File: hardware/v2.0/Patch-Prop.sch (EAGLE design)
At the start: 47 parts, among them IC1 TPS77033, IC2 XBEE, IC3 MMA8452Q, IC4 ATMEGA168, IC5 MCP1253, IC6 W2RV005RM, U2 MCP73831, X1 USBSMD

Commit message: Tweaking route style and doing cleanup
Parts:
- renumbered D1 to MOCW
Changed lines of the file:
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@@
 <part name="SUPPLY7" library="supply2" deviceset="V+" device=""/>
 <part name="SUPPLY8" library="supply2" deviceset="V+" device=""/>
-<part name="D1" library="led" deviceset="LED" device="CHIPLED_0805"/>
+<part name="MOCW" library="led" deviceset="LED" device="CHIPLED_0805"/>
 <part name="R2" library="rcl" deviceset="R-US_" device="R0603" value="470"/>
 <part name="R4" library="rcl" deviceset="R-US_" device="R0603" value="2k"/>
@@
 <instance part="SUPPLY7" gate="1" x="401.32" y="129.54"/>
 <instance part="SUPPLY8" gate="1" x="515.62" y="106.68"/>
-<instance part="D1" gate="G$1" x="81.28" y="345.44" rot="R90"/>
+<instance part="MOCW" gate="G$1" x="81.28" y="345.44" rot="R90"/>
 <instance part="R2" gate="G$1" x="93.98" y="345.44" rot="R180"/>
 <instance part="R4" gate="G$1" x="132.08" y="327.66" rot="R270"/>
@@
 <pinref part="U2" gate="G$1" pin="VIN"/>
 <pinref part="C16" gate="G$1" pin="1"/>
-<pinref part="D1" gate="G$1" pin="A"/>
+<pinref part="MOCW" gate="G$1" pin="A"/>
 <wire x1="78.74" y1="345.44" x2="76.2" y2="345.44" width="0.1524" layer="91"/>
 <wire x1="76.2" y1="345.44" x2="76.2" y2="337.82" width="0.1524" layer="91"/>
@@
 <segment>
 <wire x1="88.9" y1="345.44" x2="86.36" y2="345.44" width="0.1524" layer="91"/>
-<pinref part="D1" gate="G$1" pin="C"/>
+<pinref part="MOCW" gate="G$1" pin="C"/>
 <pinref part="R2" gate="G$1" pin="2"/>
 </segment>

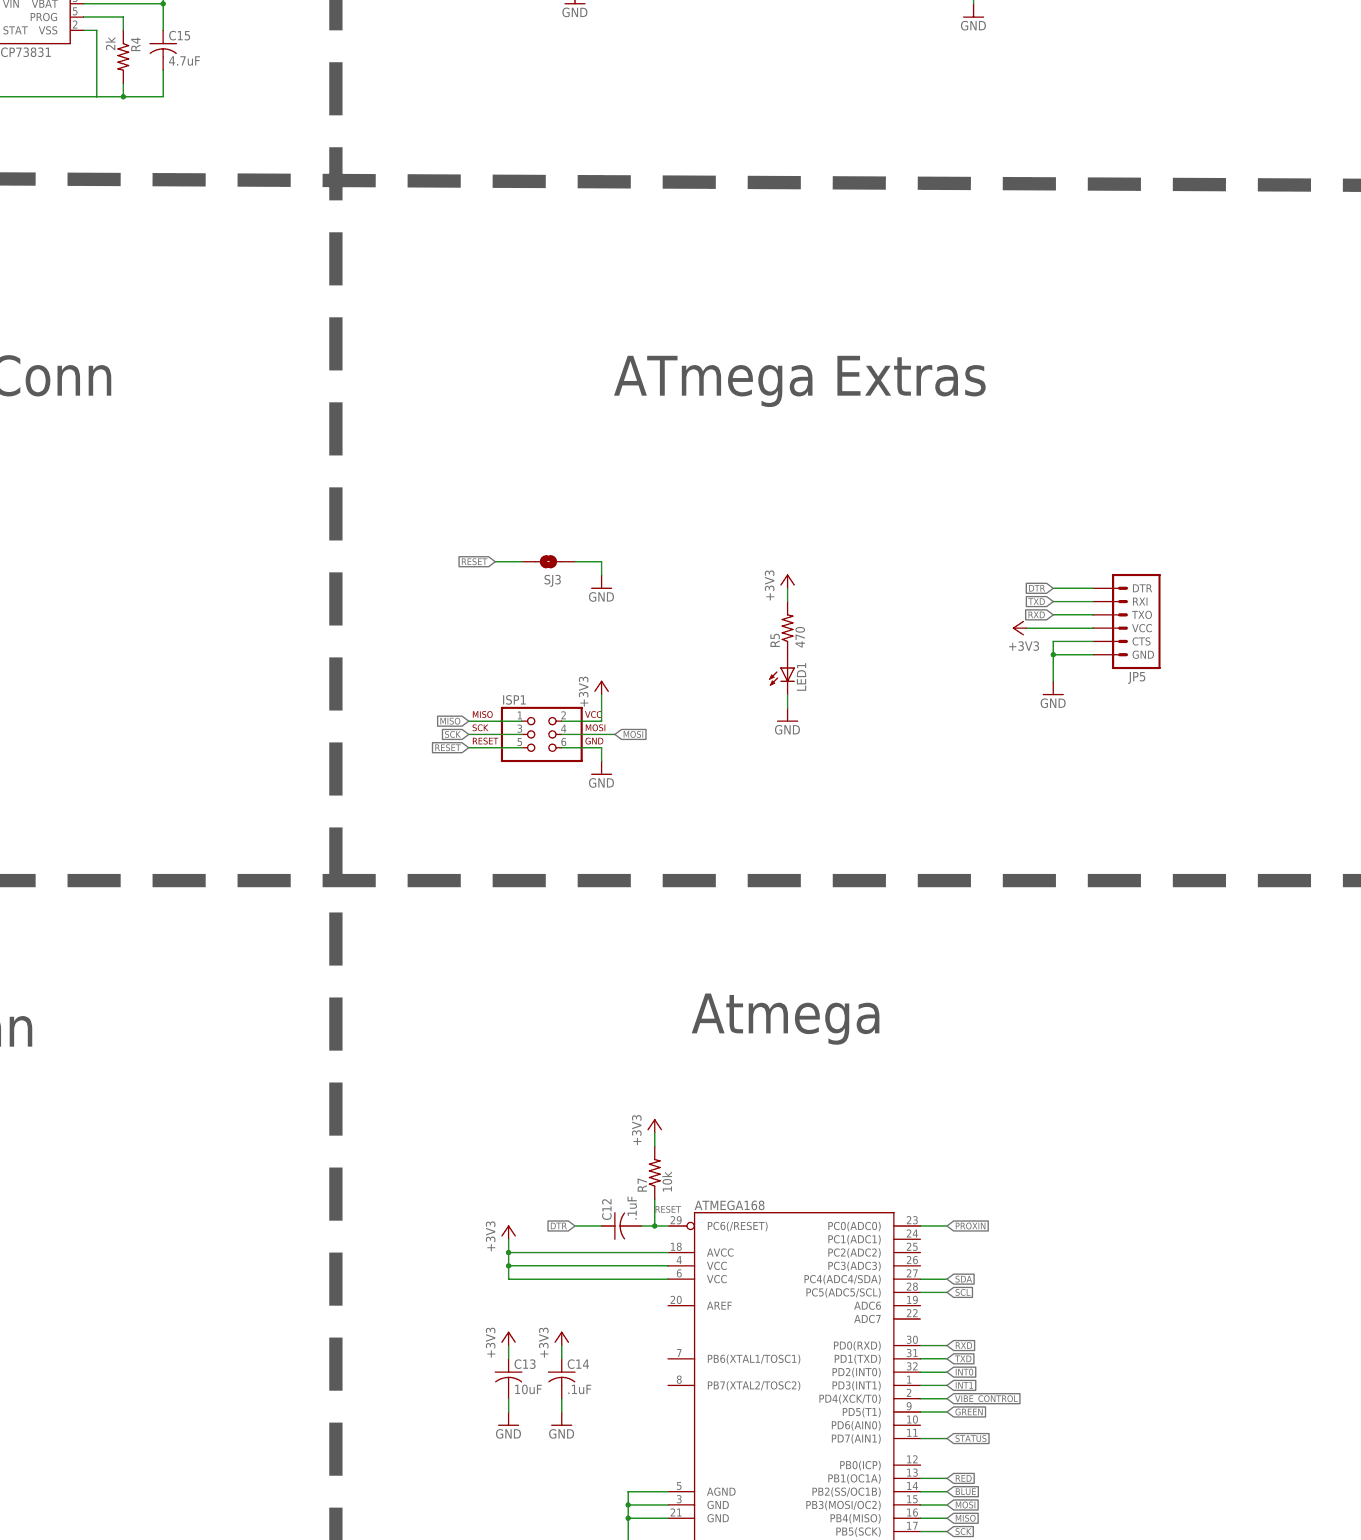
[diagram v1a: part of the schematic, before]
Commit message: Expanded board to fit mounting holes. Used extra space for breakout pins
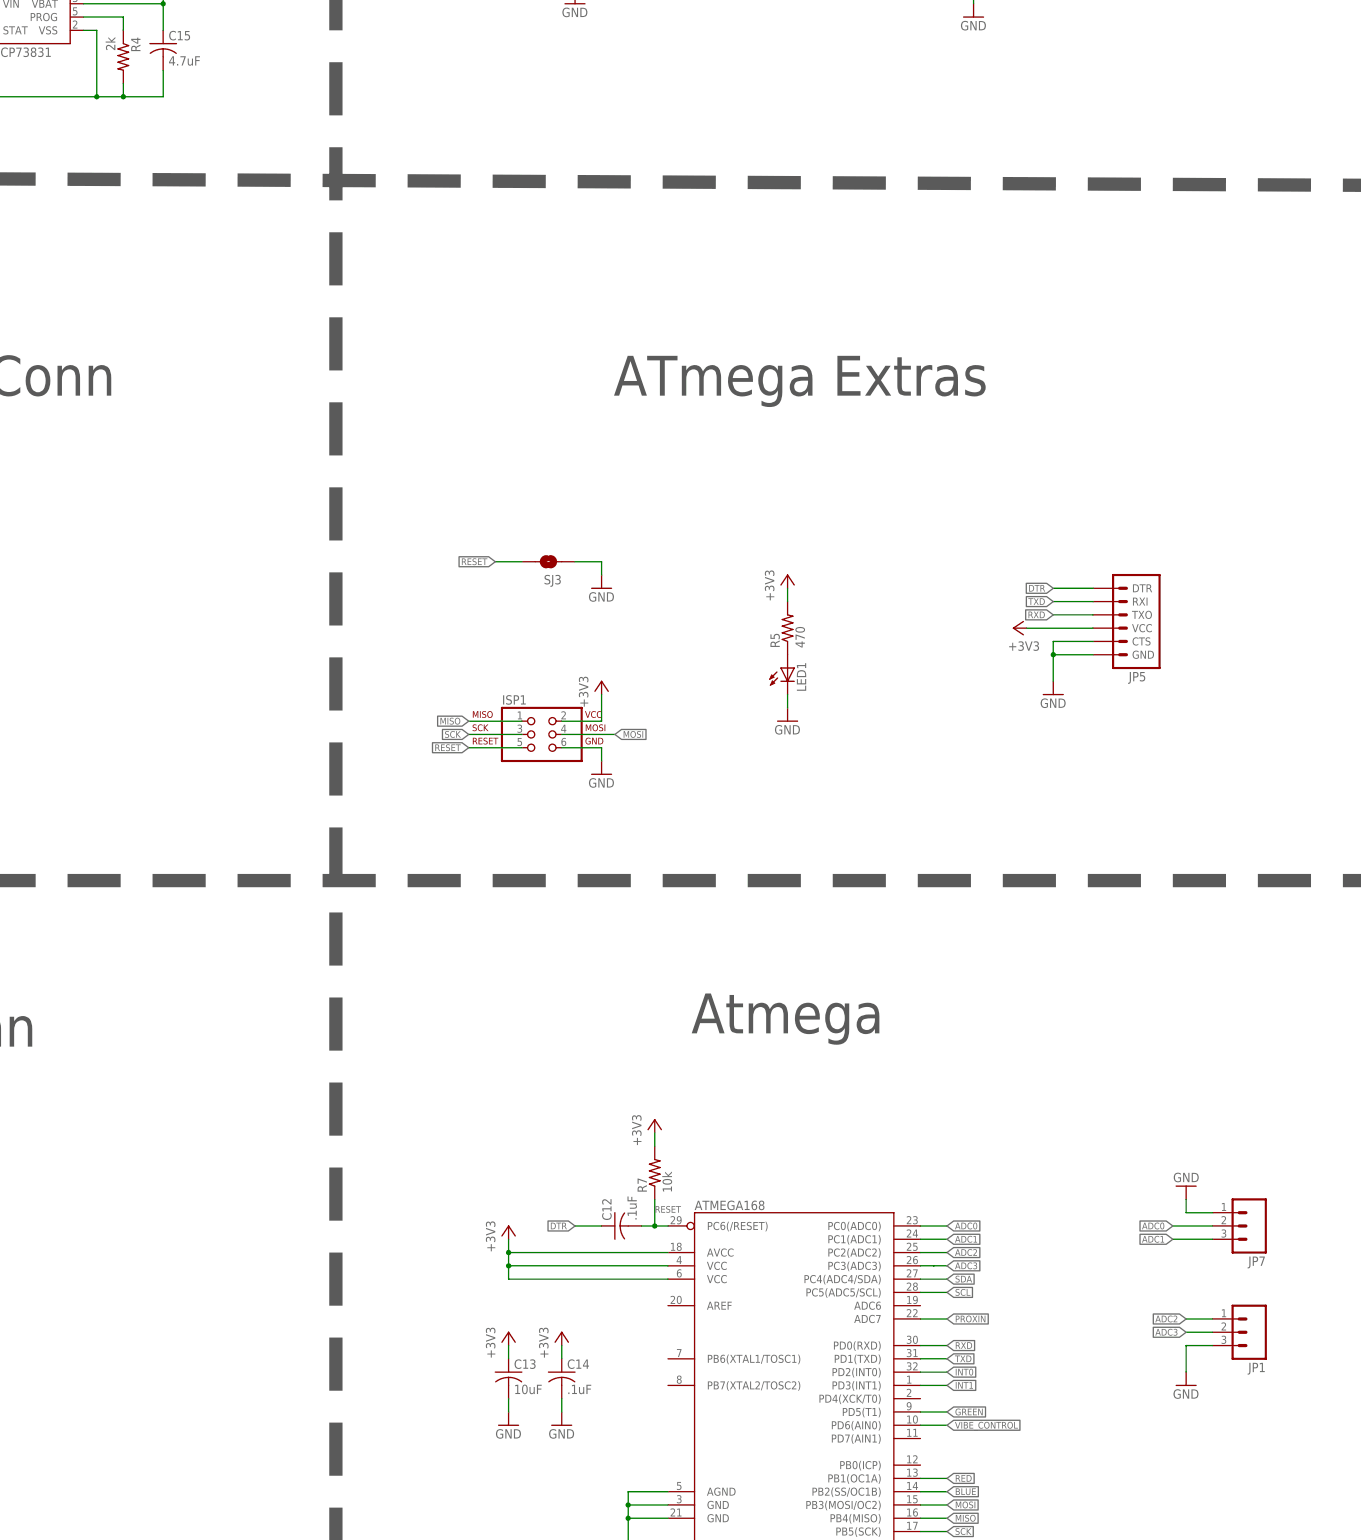
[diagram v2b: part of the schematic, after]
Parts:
- added JP1, JP7: (no value), SparkFun:M03PTH
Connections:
- removed net STATUS: IC4.PD7(AIN1)
- new net ADC0: IC4.PC0(ADC0), JP7.2
- new net ADC1: IC4.PC1(ADC1), JP7.3
- new net ADC2: IC4.PC2(ADC2), JP1.1
- new net ADC3: IC4.PC3(ADC3), JP1.2
- net GND: now also JP1.3, JP7.1
- net PROXIN: now also IC4.ADC7; no longer IC4.PC0(ADC0)
- net VIBE_CONTROL: now also IC4.PD6(AIN0); no longer IC4.PD4(XCK/T0)
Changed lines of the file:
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@@
 <part name="R9" library="rcl" deviceset="R-US_" device="R0603" value="4.7k"/>
 <part name="R10" library="rcl" deviceset="R-US_" device="R0603" value="4.7k"/>
+<part name="JP7" library="SparkFun" deviceset="M03" device="PTH"/>
+<part name="GND2" library="supply1" deviceset="GND" device=""/>
+<part name="JP1" library="SparkFun" deviceset="M03" device="PTH"/>
+<part name="GND3" library="supply1" deviceset="GND" device=""/>
 </parts>
 <sheets>
@@
 <instance part="R9" gate="G$1" x="467.36" y="88.9" rot="R180"/>
 <instance part="R10" gate="G$1" x="467.36" y="93.98" rot="R180"/>
+<instance part="JP7" gate="G$1" x="347.98" y="104.14" rot="R180"/>
+<instance part="GND2" gate="1" x="335.28" y="111.76" rot="R180"/>
+<instance part="JP1" gate="G$1" x="347.98" y="83.82" rot="R180"/>
+<instance part="GND3" gate="1" x="335.28" y="73.66"/>
 </instances>
 <busses>
@@
 <pinref part="U2" gate="G$1" pin="VSS"/>
 <wire x1="127" y1="332.74" x2="127" y2="320.04" width="0.1524" layer="91"/>
+<junction x="127" y="320.04"/>
 </segment>
 <segment>
@@
 <pinref part="GND10" gate="1" pin="GND"/>
 <wire x1="88.9" y1="78.74" x2="88.9" y2="76.2" width="0.1524" layer="91"/>
+</segment>
+<segment>
+<pinref part="JP7" gate="G$1" pin="1"/>
+<pinref part="GND2" gate="1" pin="GND"/>
+<wire x1="340.36" y1="106.68" x2="335.28" y2="106.68" width="0.1524" layer="91"/>
+<wire x1="335.28" y1="106.68" x2="335.28" y2="109.22" width="0.1524" layer="91"/>
+</segment>
+<segment>
+<pinref part="JP1" gate="G$1" pin="3"/>
+<wire x1="340.36" y1="81.28" x2="335.28" y2="81.28" width="0.1524" layer="91"/>
+<wire x1="335.28" y1="81.28" x2="335.28" y2="76.2" width="0.1524" layer="91"/>
+<pinref part="GND3" gate="1" pin="GND"/>
 </segment>
 </net>
@@
 </segment>
 </net>
-<net name="STATUS" class="0">
-<segment>
-<pinref part="IC4" gate="G$1" pin="PD7(AIN1)"/>
-<wire x1="284.48" y1="63.5" x2="289.56" y2="63.5" width="0.1524" layer="91"/>
-<label x="289.56" y="63.5" size="1.27" layer="95" font="vector" ratio="15" xref="yes"/>
-</segment>
-</net>
 <net name="MOSI" class="0">
 <segment>
@@
 </segment>
 <segment>
-<pinref part="IC4" gate="G$1" pin="PC0(ADC0)"/>
-<wire x1="284.48" y1="104.14" x2="289.56" y2="104.14" width="0.1524" layer="91"/>
-<label x="289.56" y="104.14" size="1.27" layer="95" font="vector" ratio="15" xref="yes"/>
+<pinref part="IC4" gate="G$1" pin="ADC7"/>
+<wire x1="284.48" y1="86.36" x2="289.56" y2="86.36" width="0.1524" layer="91"/>
+<label x="289.56" y="86.36" size="1.27" layer="95" font="vector" ratio="15" xref="yes"/>
 </segment>
 </net>
@@
 </segment>
 <segment>
-<pinref part="IC4" gate="G$1" pin="PD4(XCK/T0)"/>
-<wire x1="284.48" y1="71.12" x2="289.56" y2="71.12" width="0.1524" layer="91"/>
-<label x="289.56" y="71.12" size="1.27" layer="95" font="vector" ratio="14" xref="yes"/>
+<pinref part="IC4" gate="G$1" pin="PD6(AIN0)"/>
+<wire x1="284.48" y1="66.04" x2="289.56" y2="66.04" width="0.1524" layer="91"/>
+<label x="289.56" y="66.04" size="1.27" layer="95" font="vector" ratio="15" xref="yes"/>
 </segment>
 </net>
@@
 </segment>
 </net>
+<net name="ADC1" class="0">
+<segment>
+<pinref part="JP7" gate="G$1" pin="3"/>
+<label x="332.74" y="101.6" size="1.27" layer="95" font="vector" ratio="15" rot="R180" xref="yes"/>
+<wire x1="332.74" y1="101.6" x2="340.36" y2="101.6" width="0.1524" layer="91"/>
+</segment>
+<segment>
+<pinref part="IC4" gate="G$1" pin="PC1(ADC1)"/>
+<wire x1="284.48" y1="101.6" x2="289.56" y2="101.6" width="0.1524" layer="91"/>
+<label x="289.56" y="101.6" size="1.27" layer="95" font="vector" ratio="15" xref="yes"/>
+</segment>
+</net>
+<net name="ADC0" class="0">
+<segment>
+<pinref part="JP7" gate="G$1" pin="2"/>
+<wire x1="340.36" y1="104.14" x2="332.74" y2="104.14" width="0.1524" layer="91"/>
+<label x="332.74" y="104.14" size="1.27" layer="95" font="vector" ratio="15" rot="R180" xref="yes"/>
+</segment>
+<segment>
+<pinref part="IC4" gate="G$1" pin="PC0(ADC0)"/>
+<wire x1="289.56" y1="104.14" x2="284.48" y2="104.14" width="0.1524" layer="91"/>
+<label x="289.56" y="104.14" size="1.27" layer="95" font="vector" ratio="15" xref="yes"/>
+</segment>
+</net>
+<net name="ADC2" class="0">
+<segment>
+<pinref part="IC4" gate="G$1" pin="PC2(ADC2)"/>
+<wire x1="284.48" y1="99.06" x2="289.56" y2="99.06" width="0.1524" layer="91"/>
+<label x="289.56" y="99.06" size="1.27" layer="95" font="vector" ratio="15" xref="yes"/>
+</segment>
+<segment>
+<wire x1="340.36" y1="86.36" x2="335.28" y2="86.36" width="0.1524" layer="91"/>
+<label x="335.28" y="86.36" size="1.27" layer="95" font="vector" ratio="15" rot="R180" xref="yes"/>
+<pinref part="JP1" gate="G$1" pin="1"/>
+</segment>
+</net>
+<net name="ADC3" class="0">
+<segment>
+<wire x1="287.02" y1="96.52" x2="289.56" y2="96.52" width="0.1524" layer="91"/>
+<pinref part="IC4" gate="G$1" pin="PC3(ADC3)"/>
+<wire x1="287.02" y1="96.52" x2="284.48" y2="96.52" width="0.1524" layer="91"/>
+<label x="289.56" y="96.52" size="1.27" layer="95" font="vector" ratio="15" xref="yes"/>
+</segment>
+<segment>
+<wire x1="340.36" y1="83.82" x2="335.28" y2="83.82" width="0.1524" layer="91"/>
+<label x="335.28" y="83.82" size="1.27" layer="95" font="vector" ratio="15" rot="R180" xref="yes"/>
+<pinref part="JP1" gate="G$1" pin="2"/>
+</segment>
+</net>

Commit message: Smashed and adjusted part names, added pin annotation
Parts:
- removed C15, C16: 4.7uF, rcl:C-USC0603
- removed IC4: ATMEGA168, SparkFun:ATMEGA168
- removed LED6: RGBLED5050, adafruit:RGBLED5050
- removed R10: 4.7k, rcl:R-US_R0603
- removed SJ3: SOLDERJUMPERNO, SparkFun:SOLDERJUMPERNO
- added C6: .1uF, rcl:C-USC0603
- added C8: 10uF, rcl:C-USC0603
- added LED2: RGBLED5050, adafruit:RGBLED5050
- added R3: 2k, rcl:R-US_R0603
- added SJ2: SOLDERJUMPERNO, SparkFun:SOLDERJUMPERNO
- added XBEE: XBEE, adafruit:XBEE
- C1: value 1uF -> 4.7uF
- C10: value 0.1uF -> 10uF
- C11: value 4.7uF -> 0.1uF
- C12: value .1uF -> 0.1uF
- C13: value 10uF -> 4.7uF
- C14: value .1uF -> 4.7uF
- C5: value 10uF -> .1uF
- C9: value 0.1uF -> 1uF
- IC2: value XBEE -> ATMEGA168; device adafruit:XBEE -> SparkFun:ATMEGA168
- IC3: value MMA8452Q -> MCP1253; device eski-ic:MMA8452Q -> CH_Microchip:MCP1253
- IC5: value MCP1253 -> MMA8452Q; device CH_Microchip:MCP1253 -> eski-ic:MMA8452Q
- R1: value 100k -> RLim
- R4: value 2k -> 10k
- R6: value RLim -> 100k
- R7: value 10k -> 4.7k
- renumbered ISP1 to ICSP, JP1 to IO1, JP2 to BATT, JP3 to PROX, JP5 to FTDI, JP6 to VIBE, JP7 to IO2, LED1 to PWR, MOCW to CHRG, T2 to T1, U2 to IC7, X1 to USB
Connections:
- net +3V3: now also C5.1, C7.1, C8.1, IC2.AVCC, IC2.VCC@1, IC2.VCC@2, IC3./SHDN, IC3.VIN, IC5.VDD, IC5.VDDIO, R4.2, XBEE.VCC; no longer C14.1, C2.1, C9.1, IC2.VCC, IC3.VDD, IC3.VDDIO, IC4.AVCC, IC4.VCC@1, IC4.VCC@2, IC5./SHDN, IC5.VIN, R7.2
- net ADC0: now also IC2.PC0(ADC0); no longer IC4.PC0(ADC0)
- net ADC1: now also IC2.PC1(ADC1); no longer IC4.PC1(ADC1)
- net ADC2: now also IC2.PC2(ADC2); no longer IC4.PC2(ADC2)
- net ADC3: now also IC2.PC3(ADC3); no longer IC4.PC3(ADC3)
- net BLUE: now also IC2.PB2(SS/OC1B), R7.2; no longer IC4.PB2(SS/OC1B), R8.2
- net BLUE_OUT: now also LED2.BLUE_C; no longer LED6.BLUE_C
- net DTR: now also C6.1; no longer C12.1
- net GND: now also C1.2, C12.2, C8.2, IC2.AGND, IC2.GND@1, IC2.GND@2, IC3.GND, IC3.SELECT, IC5.GND1, IC5.GND2, IC5.GND3, IC5.SA0, R1.1, R3.2, SJ1.1, XBEE.GND; no longer C15.2, C16.2, C9.2, IC2.GND, IC3.GND1, IC3.GND2, IC3.GND3, IC3.SA0, IC4.AGND, IC4.GND@1, IC4.GND@2, IC5.GND, IC5.SELECT, R4.2, R6.1, SJ3.1
- net GREEN: now also IC2.PD5(T1); no longer IC4.PD5(T1)
- net GREEN_OUT: now also LED2.GREEN_C; no longer LED6.GREEN_C
- net INT0: now also IC2.PD2(INT0), IC5.INT1; no longer IC3.INT1, IC4.PD2(INT0)
- net INT1: now also IC2.PD3(INT1), IC5.INT2; no longer IC3.INT2, IC4.PD3(INT1)
- net MISO: now also IC2.PB4(MISO); no longer IC4.PB4(MISO)
- net MOSI: now also IC2.PB3(MOSI/OC2); no longer IC4.PB3(MOSI/OC2)
- net N$10: now also C10.1, IC3.VOUT, R6.1; no longer C5.1, IC5.VOUT, R1.1
- net N$11: now also R3.1; no longer R4.1
- net N$16: now also C12.1, IC5.BYP; no longer C10.1, IC3.BYP
- net N$19: now also SJ2.1, XBEE.RESET; no longer IC2.RESET, SJ1.1
- net N$3: now also C9.1, IC3.C-; no longer C1.1, IC5.C-
- net N$4: now also R1.2; no longer R6.2
- net N$6: now also C9.2, IC3.C+; no longer C1.2, IC5.C+
- net N$7: now also R7.1; no longer R8.1
- net N$9: now also R8.1; no longer R10.1
- net PGOOD: now also IC3.PGOOD, R6.2; no longer IC5.PGOOD, R1.2
- net PROXIN: now also IC2.ADC7; no longer IC4.ADC7
- net RED: now also IC2.PB1(OC1A), R8.2; no longer IC4.PB1(OC1A), R10.2
- net RED_OUT: now also LED2.RED_C; no longer LED6.RED_C
- net RESET: now also C6.2, IC2.PC6(/RESET), R4.1, SJ2.2; no longer C12.2, IC4.PC6(/RESET), R7.1, SJ3.2
- net RXD: now also IC2.PD0(RXD), XBEE.DOUT; no longer IC2.DOUT, IC4.PD0(RXD)
- net SCK: now also IC2.PB5(SCK); no longer IC4.PB5(SCK)
- net SCL: now also IC2.PC5(ADC5/SCL), IC5.SCL; no longer IC3.SCL, IC4.PC5(ADC5/SCL)
- net SDA: now also IC2.PC4(ADC4/SDA), IC5.SDA; no longer IC3.SDA, IC4.PC4(ADC4/SDA)
- net TXD: now also IC2.PD1(TXD), XBEE.DIN; no longer IC2.DIN, IC4.PD1(TXD)
- net USB_VIN: now also C1.1; no longer C16.1
- net V+: now also C14.1, C2.1, LED2.BLUE_A, LED2.GREEN_A, LED2.RED_A; no longer C15.1, C7.1, LED6.BLUE_A, LED6.GREEN_A, LED6.RED_A
- net VIBE_CONTROL: now also IC2.PD6(AIN0); no longer IC4.PD6(AIN0)
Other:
- moved on the sheet: C1, C10, C11, C12, C13, C14, C2, C4, C5, C7, C9, LED3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
